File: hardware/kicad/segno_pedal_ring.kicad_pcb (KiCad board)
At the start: 2 copper layers, 60 x 60 mm, 13 parts, among them J1 JST-XH 8P, J2 NEOPIXEL, J3 RINGPINS

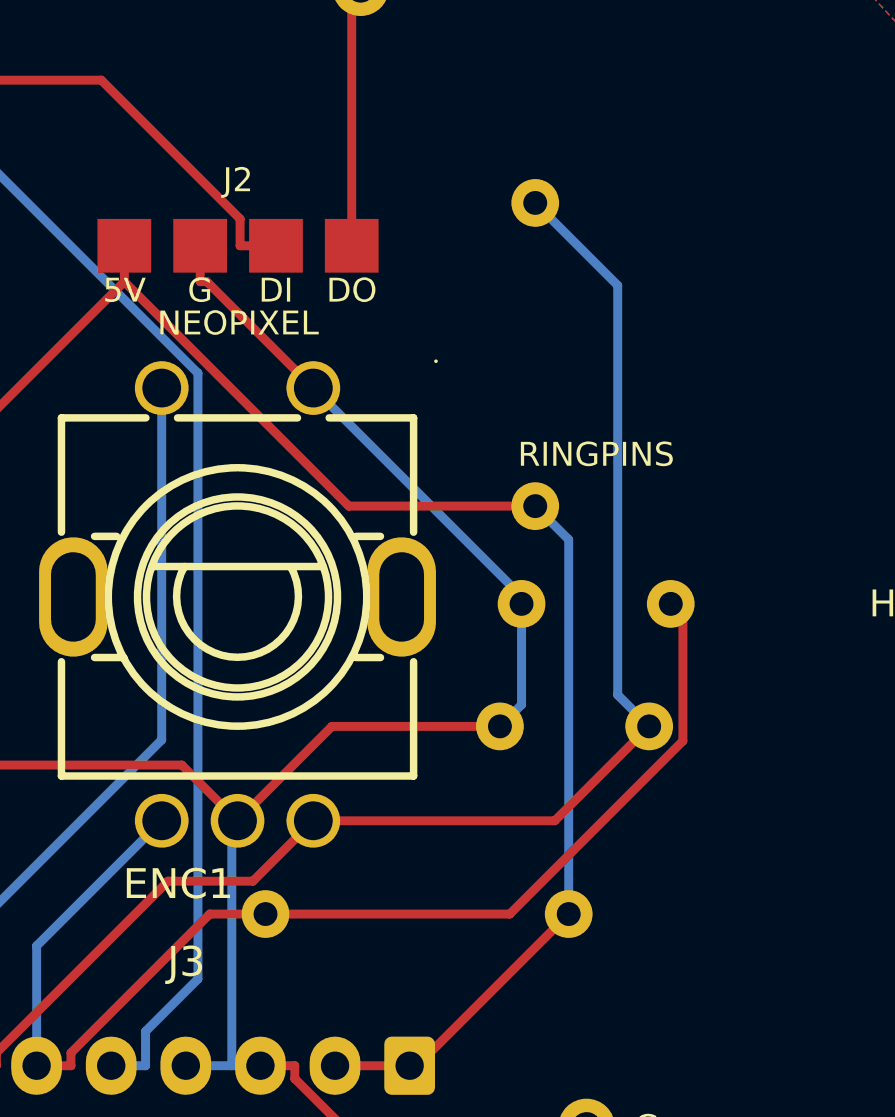
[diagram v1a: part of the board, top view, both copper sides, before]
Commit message: fix(hardware): review round 2 -- the ring surgery that never happened, and gates that need no classifier
Round 2 of the review loop, four fresh angles over round 1's work. The
headline finding is about round 1 itself.

THE RING SURGERY WAS A PHANTOM. Round 1's commit claimed R1/R2 removed from
segno_pedal_ring.kicad_pcb with healing vias -- but the surgery script had
crashed with its stderr swallowed, an unchained DRC then measured the
restored ORIGINAL board's clean baseline, and the false green shipped: the
committed PCB still carried both pull-up footprints, zero vias, and gerbers
copper-identical to the stale zip. Redone with absolute paths, visible
errors, and the assertions chained: R1/R2 are gone, two 0.4 mm vias stand at
the exact rail pad centres (the through-pads doubled as the +5V_LED layer
transitions -- and the board had no other vias, which is what killed the
crashed attempt's clone-a-via approach), DRC refills to 0/0, and the drill
file is verified BY TOOL DIAMETER to carry the vias and not the component
holes. The lesson is committed as method: every artifact claim in this round
is asserted from the artifact, not from the log that produced it.

THE GATES DROP THEIR CLASSIFIERS. RING_LEVELS judged bridging parts by
footprint lib or value pattern -- fail-open on custom libs and suffixed
values, as review proved. The rule is now classification-free on both boards:
any TWO-PIN part bridging the rail to a protected line delivers the rail's DC
whatever it calls itself (resistor, 0R, ferrite, cap), and the pin count
comes from the netlist, so J1 and the ICs are exempt by arithmetic instead of
by name. CONSOLE_LEVELS gets the same rule (it had shipped with the weaker
footprint test the same commit had just deprecated on the ring side).
PIN_REFS asserts nets as well as value -- the recorded usurper was itself a
10k, so value alone could not tell the stolen name from the real part.
parse_netlist refuses duplicate net names (git text-merge damage would
otherwis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
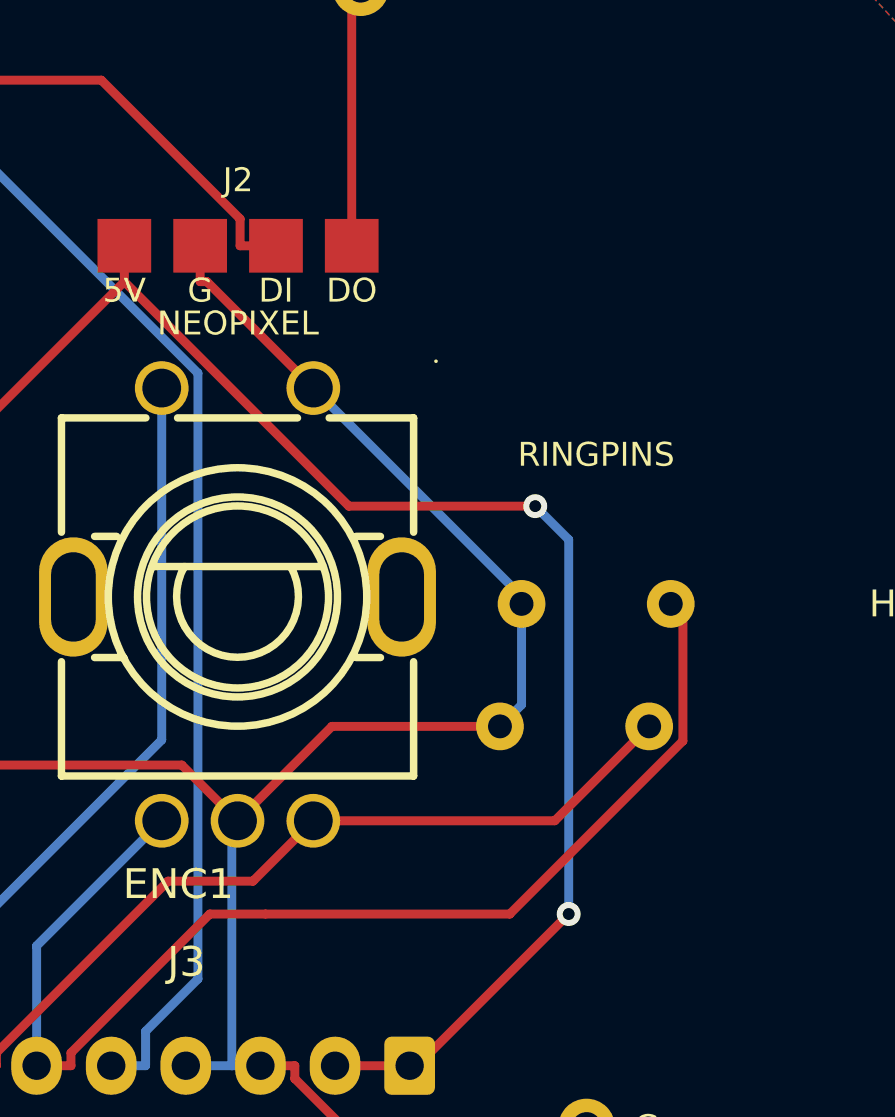
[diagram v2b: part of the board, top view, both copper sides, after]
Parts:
- removed R1, R2: 10k, R_Axial_DIN0207_L6.3mm_D2.5mm_P10.16mm_Horizontal
- C1: value 470uF -> 470uF 16V low-ESR <=0.15R
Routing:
- net ENC_B: track 47.1 -> 28.0 mm
- net +5V_LED: vias 0 -> 2

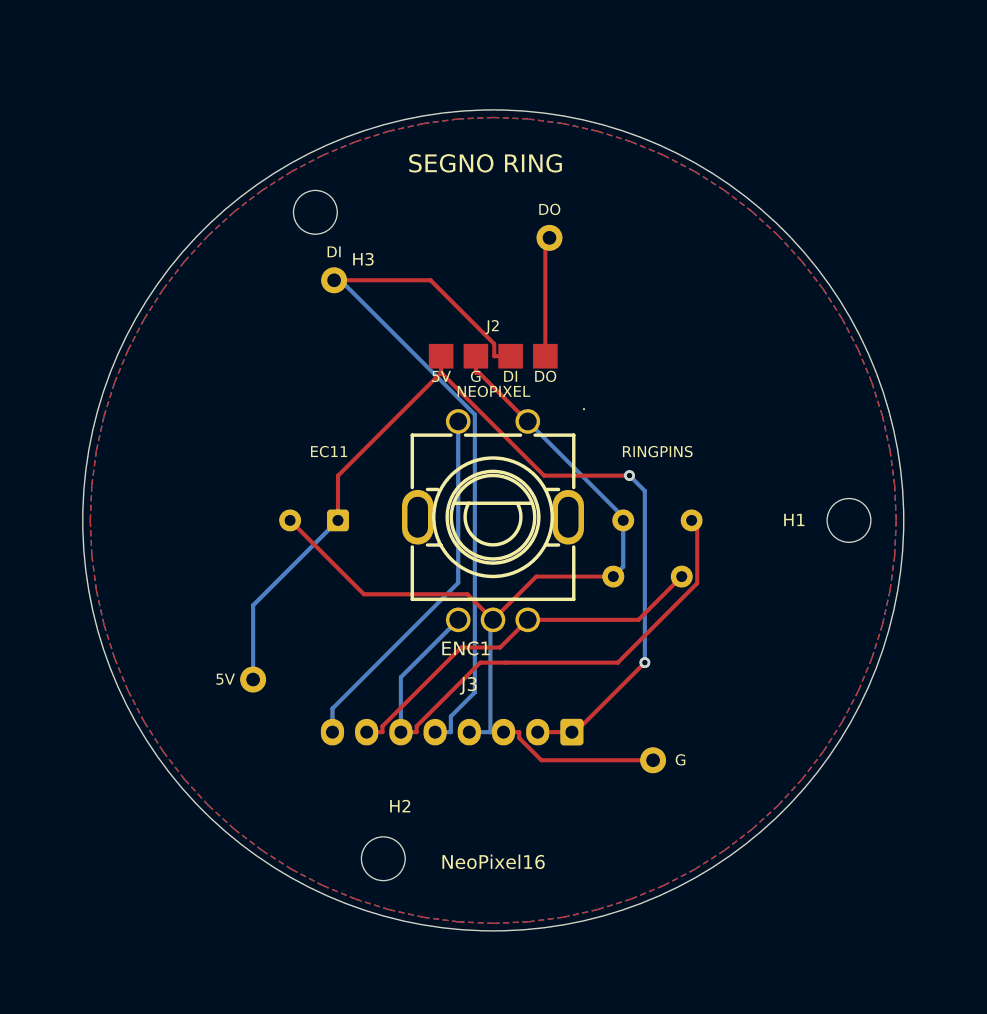
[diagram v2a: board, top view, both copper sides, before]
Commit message: feat(hardware): re-cut the ring board for the Ring 24 (#794)
The board was still a Ring 16 design. A O65.5 ring on a O60 board overhangs the
PCB by 2.75 mm all round, so this was mechanical, not cosmetic.

OUTLINE O60 -> O68. Enough to carry the ring with ~1 mm of land outside it.

MOUNT HOLES r=26 -> r=22, into the ring's O52.3 bore. At r=26 they sat 0.15 mm
from the ring's inner edge: the M3 heads fouled it and were unreachable once the
ring was on. Inboard, an O6 head reaches r=25 and clears by 1.15 mm, and the
screws stay accessible through the bore during assembly (before disc and knob).

Angles are 36.5 / 163.2 / 258.9, not the tidy 0 / 120 / 240 they look like they
should be. Those are the midpoints of the three widest PAD-FREE angular gaps in
the r>=14 band, and they were found the hard way -- DRC caught 240 landing on
J3's DI pad and 120 sitting inside J1's pad fan (which runs 69.6 to 127.2 deg).
Anything that moves a pad on this board has to re-check that map.

RING1 -> NeoPixel_Ring24, a new documentation-only footprint (O65.5 / O52.3 doc
circles, no pads, no courtyard -- a O65.5 courtyard swallows every part on a O68
board and DRC reports 27 phantom pth_inside_courtyard). Deliberately no 3D model:
the Ring 16's NeoPixel_PCB.wrl is the wrong diameter, and a wrongly-sized model
is worse than none.

J3 IS KEPT BUT CANNOT BE USED WITH THIS RING. Its pads are a O42.1 circle, inside
the Ring 24's O52.3 bore, so they land in open air. The ring connects through J2
(WirePads_1x04, same nets, three wires). J3 stays because it is on the right
nets, costs nothing, still serves a Ring 16 build, and deleting it would mean
re-routing four nets for no functional gain -- but ring_board.py and the
footprint's own descr now say so plainly. A Ring 24 pad circle needs the four pad
centres measured off the physical part; that is still open on #794.

Verified: DRC 0 violations, 0 unconnected. Ring annulus r 26.15..32.75 is clear
of every pad on the board (outermost is r=22.00)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
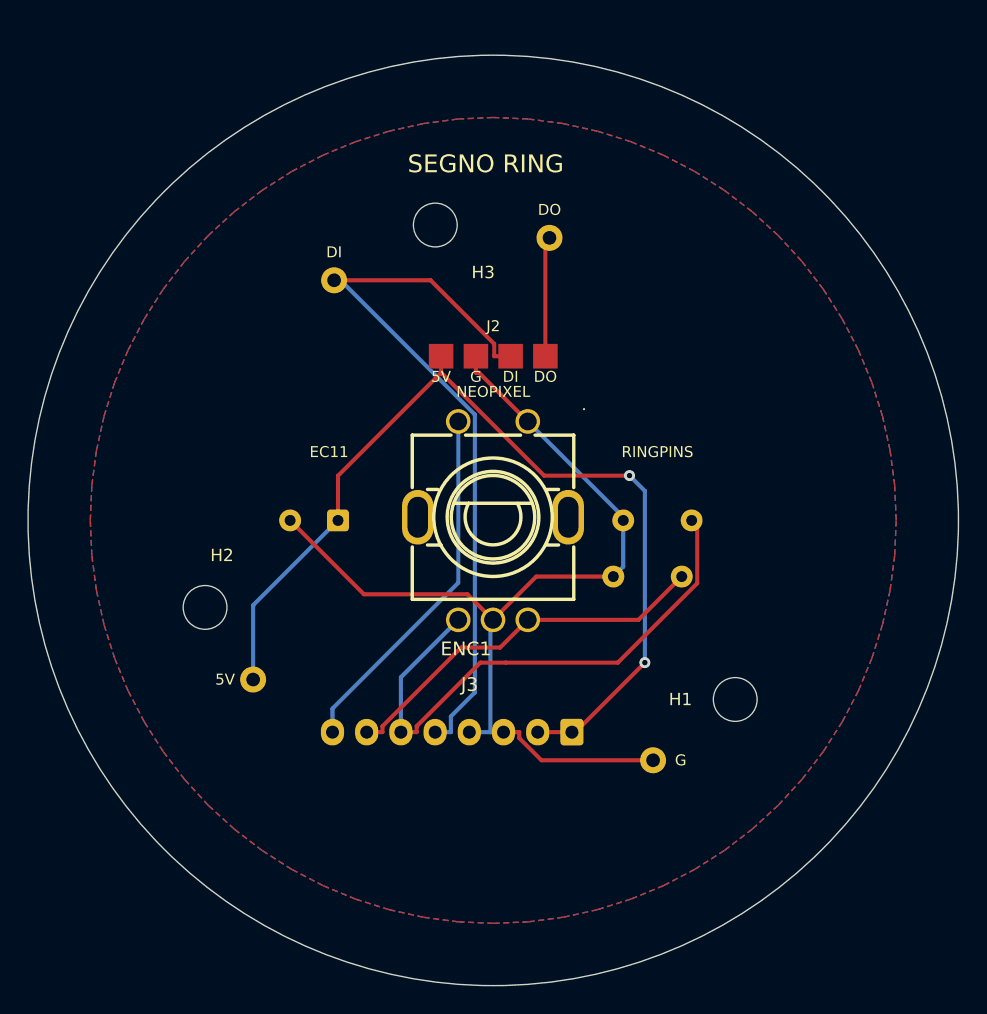
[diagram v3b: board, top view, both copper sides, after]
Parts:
- RING1: value NeoPixel16 -> NeoPixel24; footprint NeoPixel_Ring16 -> NeoPixel_Ring24
- moved H2 22.5 mm to (14.9, 42.4)
- moved H1 15.5 mm to (53.7, 49.1)
- moved H3 8.81 mm to (31.8, 14.4)
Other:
- board size 60 x 60 mm -> 68 x 68 mm
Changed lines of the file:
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@@
 	(footprint "MountingHole_3.2mm_M3"
 		(layer "F.Cu")
-		(at 23 13.4833)
+		(at 31.764516 14.411561)
 		(descr "Mounting Hole 3.2mm, M3, no annular, generated by kicad-footprint-generator mountinghole.py")
 		(tags "mountinghole M3")
@@
 	(footprint "MountingHole_3.2mm_M3"
 		(layer "F.Cu")
-		(at 27.9656 60.7275)
+		(at 14.938971 42.358699)
 		(descr "Mounting Hole 3.2mm, M3, no annular, generated by kicad-footprint-generator mountinghole.py")
 		(tags "mountinghole M3")
@@
 	(footprint "MountingHole_3.2mm_M3"
 		(layer "F.Cu")
-		(at 62 36)
+		(at 53.68485 49.086101)
 		(descr "Mounting Hole 3.2mm, M3, no annular, generated by kicad-footprint-generator mountinghole.py")
 		(tags "mountinghole M3")
@@
 		(embedded_fonts no)
 	)
-	(footprint "NeoPixel_Ring16"
+	(footprint "NeoPixel_Ring24"
 		(layer "F.Cu")
 		(at 36 36)
-		(descr "Adafruit NeoPixel Ring 16 (geometry from Adafruit .brd): black PCB with 4 cut THT holes (two-sided copper pads), 16 LEDs, 3 mount pins to J3.")
+		(descr "NeoPixel Ring 24 module, O65.5 OD / O52.3 ID / 3.2 thick -- the fitted part (#794). DOCUMENTATION ONLY: no pads. The module connects through J2 (WirePads_1x04) by flying wires; the Ring-16-era pin-mount pads (J3/ModuleMountPads_4) do NOT line up with this ring and are not used. No 3D model: the Ring 16's NeoPixel_PCB.wrl is the wrong diameter and a wrongly-sized model is worse than none.")
 		(property "Reference" "RING1"
-			(at 0 -25 0)
+			(at 0 -35 0)
 			(layer "F.SilkS")
 			(hide yes)
@@
 			)
 		)
-		(property "Value" "NeoPixel16"
-			(at 0 25 0)
-			(layer "F.SilkS")
+		(property "Value" "NeoPixel24"
+			(at 0 35 0)
+			(layer "F.Fab")
+			(hide yes)
 			(effects
 				(font
@@
 		(fp_circle
 			(center 0 0)
-			(end 22.225 0)
+			(end 26.15 0)
 			(stroke
 				(width 0.12)
@@
 			(layer "Dwgs.User")
 		)
-		(embedded_fonts no)
-		(model "${KIPRJMOD}/segno.pretty/NeoPixel_PCB.wrl"
-			(offset
-				(xyz 0 0 7.4)
-			)
-			(scale
-				(xyz 0.3937 0.3937 0.3937)
-			)
-			(rotate
-				(xyz 0 0 0)
+		(fp_circle
+			(center 0 0)
+			(end 32.75 0)
+			(stroke
+				(width 0.12)
+				(type solid)
 			)
+			(fill no)
+			(layer "Dwgs.User")
 		)
+		(embedded_fonts no)
 	)
 	(footprint "C_Disc_D5.0mm_W2.5mm_P5.00mm"
@@
 		(tags "CP Radial series Radial pin pitch 3.50mm diameter 8mm height 12mm Electrolytic Capacitor")
 		(property "Reference" "C1"
-			(at 1.75 5.25 0)
+			(at 0.0027 5.4 0)
 			(layer "B.SilkS")
 			(effects
@@
 		)
 		(property "Value" "470uF 16V low-ESR <=0.15R"
-			(at 1.75 -5.25 0)
+			(at 3.1527 8.4 0)
 			(layer "B.SilkS")
 			(effects
 				(font
-					(size 1 1)
-					(thickness 0.15)
+					(size 0.8 0.8)
+					(thickness 0.12)
 				)
 				(justify mirror)
@@
 	(gr_circle
 		(center 36 36)
-		(end 66 36)
+		(end 70 36)
 		(stroke
 			(width 0.1)

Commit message: feat(hardware): pin-mount pads for the Ring 24, taken from Adafruit's board file
I had said this could not be done without measuring the physical ring. That was
wrong -- Adafruit publish the source, and the numbers were a download away.

github.com/adafruit/Adafruit-NeoPixel-Ring, 'Adafruit NeoPixel Ring 24 B.brd'.
That file also settles which ring this is: its Dimension layer reads O65.53 /
O52.32, matching the fitted part's 65.5 / 52.3 exactly.

WHAT WAS TAKEN, AND HOW IT WAS CHECKED. Pad centres are the JP element positions
with Y negated for KiCad's downward Y. The method was validated against the Ring
16 file FIRST: the same extraction reproduces the existing ModuleMountPads_4 pads
to the micron, so the transform is right before it is trusted on the 24.

Signals are read from the .brd netlist, not inferred from JP numbering: JP1=IN
(via R1), JP2=OUT (LED24's DOUT), JP3=VDD, JP4=GND. On the Ring 16 the nets are
literally named IN/OUT; on the 24 they are N/N, so they had to be traced
through the LED chain. Assuming JP order carries across ring sizes would have
been a silent 50/50 on DIN vs DOUT.

All four pads land at r=31.59, inside the ring's 26.16..32.77 material band, and
verified against the source to within 5 um in the finished board.

ROUTING. Moving the pads from r=21 to r=31.6 pulled four nets apart:
- the GND pour was still a r=29.45 circle cut for the O60 outline and did not
  reach the new pads -- scaled to r=33.45, keeping the original 0.55 inset;
- the old J3 DI pad had been RING_DATA's F/B layer transition, so removing it
  split the net across layers -- replaced with a via at the same point;
- RING_DATA dog-legs east of H3, whose hole it otherwise passed 0.27 mm from;
- RING_DOUT runs on B.Cu because it would cross RING_DATA on the front;
- +5V_LED widened 0.30 -> 0.55: 24 LEDs draw ~1.44 A all-white where 16 drew ~1 A.
Two GND stubs that existed only to reach the old pad were deleted; they were
redundant against the pour and were blocking the +5V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
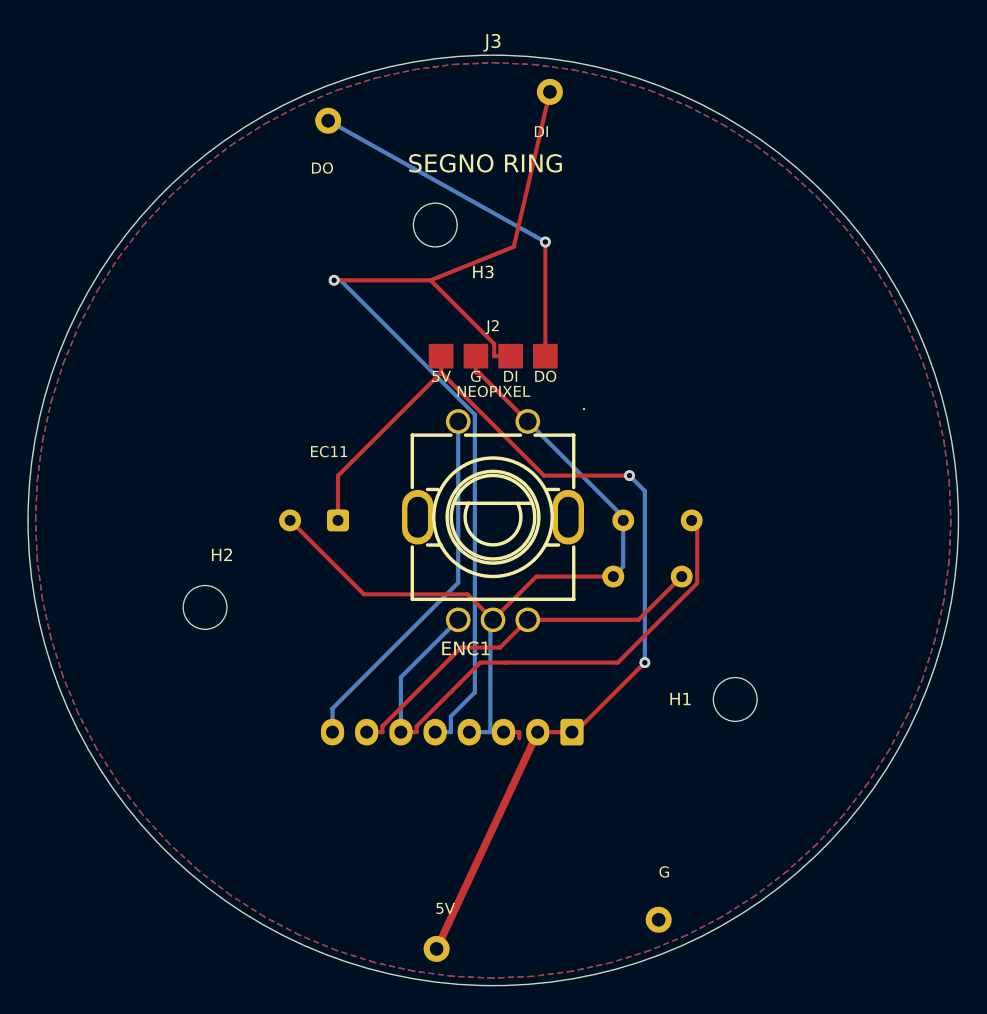
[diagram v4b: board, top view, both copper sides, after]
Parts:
- J3: value RINGPINS -> RINGPINS24; footprint ModuleMountPads_4 -> ModuleMountPads_Ring24
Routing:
- net RING_DATA: track 55.2 -> 73.3 mm, vias 0 -> 1
- net RING_DOUT: track 8.77 -> 26.5 mm, vias 0 -> 1
- net GND: track 71.8 -> 61.3 mm
- net +5V_LED: track 70.3 -> 73.6 mm
